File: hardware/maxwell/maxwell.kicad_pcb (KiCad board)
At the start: 2 copper layers, 147 x 59 mm, 127 parts, among them J1 Canbus 1, J10 SPI2_B, J11 BACKUP, J12 UART4, J14 Interconnect (Power), J15 I2C1, J16 ESP_BM, J17 ESP_PROG, J18 Interconnect (Power-Rect), J19 Interconnect (Rect), J2 SPI2_C, J20 Interconnect (uC), J3 Neopixel, J4 BOOT0, J5 SPI2_A, J6 Programmer, J7 Dynamo, J8 BOOT1, J9 Battery, Q1 DMG2302UK, Q2 DMG2302UK, Q3 DMG9926UDM, Q4 NTR1P02T1, Q5 NTR1P02T1, Q6 DMG2302UK, Q7 DMG2302UK, Q8 DMG2302UK, Q9 DMG2302UK, SW1 SW_Push, U1 MCP1501, U10 MIC39102, U11 AP9101C-SOT-25, U12 INA219AID, U13 PCF8593, U14 TPS22917, U15 LM74670-Q1, U16 LM74670-Q1, U17 LM74670-Q1, U18 LM74670-Q1, U19 LT3086IR, U2 SN65HVD233, U20 BQ21040DBVT, U3 TPS2113, U4 PCA9536D, U5 ESP-32S, U6 AD7991, U7 STM32F103RETx, U8 TLP188, U9 MCP79411-I/SN, Y1 32.768k, Y2 8M

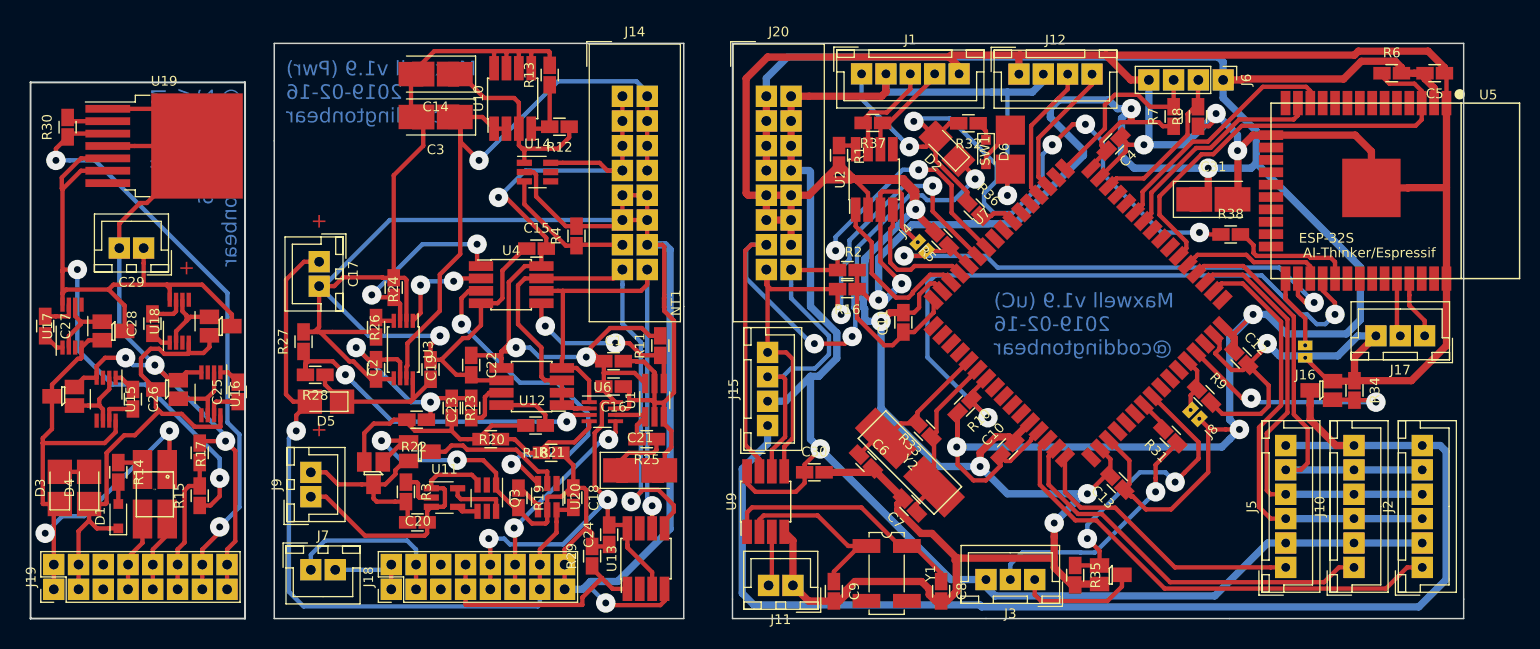
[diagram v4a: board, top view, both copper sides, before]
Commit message: Maxwell v1.9.1
While sciencing earlier today, I narrowed down my surprisingly-high
quiescent current problem to being how I've handled switching
off the Neopixels and SPI-connected devices.  Historicaly,
those were switched using a low-side N-Channel MOSFET. With these
changes, these will be switched via a high-side P-Channel MOSFET
(itself controlled by an N-Channel MOSFET to ensure that the
microcontroller isn't exposed to VCC).

* Swaps Neopixel power-off device from low-side N-Channel MOSFET
  to P-Channel MOSFET controlled by an N-Channel MOSFET.
* Swaps SPI power-off device from low-side N-Channel MOSFET
  to P-Channel MOSFET controlled by an N-Channel MOSFET.
* Fixes a few erroneous resistor values.
* Adds a diode between RTC and WAKE to prevent RTC from being
  able to turn off the power, only turn it on.

* Switches off
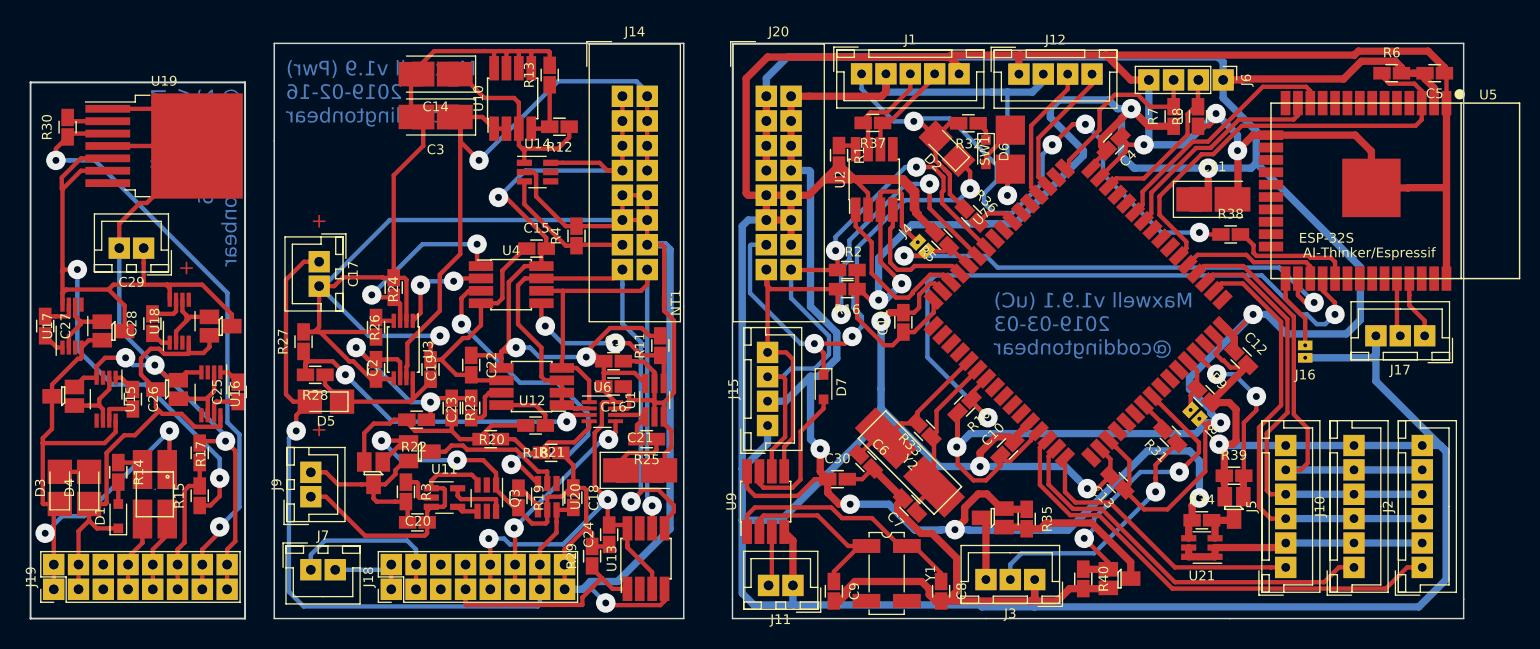
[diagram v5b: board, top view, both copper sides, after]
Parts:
- added D7: 1N4148WS, Diode_SMD:D_SOD-323_HandSoldering, F.Cu at (113.3, 108.3)
- added Q10: NDS332P, coddingtonbear:SOT-23_LargePads, F.Cu at (130.7, 121.7)
- added R39: 10k, coddingtonbear:0805_Milling, F.Cu at (155.4, 117.3)
- added R40: 10k, coddingtonbear:0805_Milling, F.Cu at (140.0, 127.9)
- added U21: STT3P2UH7, Package_TO_SOT_SMD:SOT-23-6_Handsoldering, F.Cu at (152.1, 124.7)
- D6: value D -> 1N4148WS
- R32, R36: value 10k -> 300
- moved R34 20.6 mm to (152.1, 121.9), turned to 0 degrees
- moved Q1 15.0 mm to (155.4, 120.7), turned to 270 degrees
- moved R35 7.61 mm to (134.2, 121.8)
- moved C30 2.47 mm to (114.8, 117.7)
- moved Q2 0.98 mm to (143.7, 127.9)
- moved R36 0.73 mm to (128.5, 90.7)
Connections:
- J10 pad 2: VCC_B -> Net-(J10-Pad2)
- J10 pad 6: /GNDAUX -> GND_B
- J15 pad 1: /GNDAUX -> GND_B
- J2 pad 2: VCC_B -> Net-(J10-Pad2)
- J2 pad 6: /GNDAUX -> GND_B
- J3 pad 1: Net-(J3-Pad1) -> GND_B
- J3 pad 3: VCC_B -> Net-(J3-Pad3)
- J5 pad 2: VCC_B -> Net-(J10-Pad2)
- J5 pad 6: /GNDAUX -> GND_B
- Q1 pad 3: /GNDAUX -> Net-(Q1-Pad3)
- Q2 pad 3: Net-(J3-Pad1) -> Net-(Q10-Pad1)
- R34 pad 1: GND_B -> VCC_B
- R34 pad 2: ENABLE_AUX -> Net-(Q1-Pad3)
- R35 pad 1: ENABLE_LEDS -> VCC_B
- R35 pad 2: GND_B -> Net-(Q10-Pad1)
- U9 pad 7: WAKE_B -> Net-(D7-Pad2)
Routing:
- net /GNDAUX: track 130.7 -> 0.00 mm
- net GND_B: track 453.0 -> 583.2 mm, vias 9 -> 7
- net Net-(J10-Pad2): track 0.00 -> 26.0 mm
- net WAKE_B: track 72.3 -> 50.7 mm
- net Net-(Q10-Pad1): track 0.00 -> 16.7 mm
- net Net-(D7-Pad2): track 0.00 -> 15.2 mm
- net Net-(J3-Pad1): track 12.6 -> 0.00 mm
- net Net-(J3-Pad3): track 0.00 -> 6.52 mm
- net ENABLE_AUX: track 25.1 -> 19.7 mm
- net VCC_B: track 173.9 -> 169.2 mm, vias 2 -> 5
- net Net-(Q1-Pad3): track 0.00 -> 4.34 mm
- net ESP_AVAILABLE: track 78.3 -> 74.6 mm, vias 5 -> 4
- net +3V3_B: track 350.5 -> 349.2 mm
- net Net-(R36-Pad2): track 3.64 -> 4.19 mm
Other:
- board text added: "Maxwell v1.9.1 (uC) 2019-03-03 @coddingtonbear"
- board text removed: "Maxwell v1.9 (uC) 2019-02-16 @coddingtonbear"

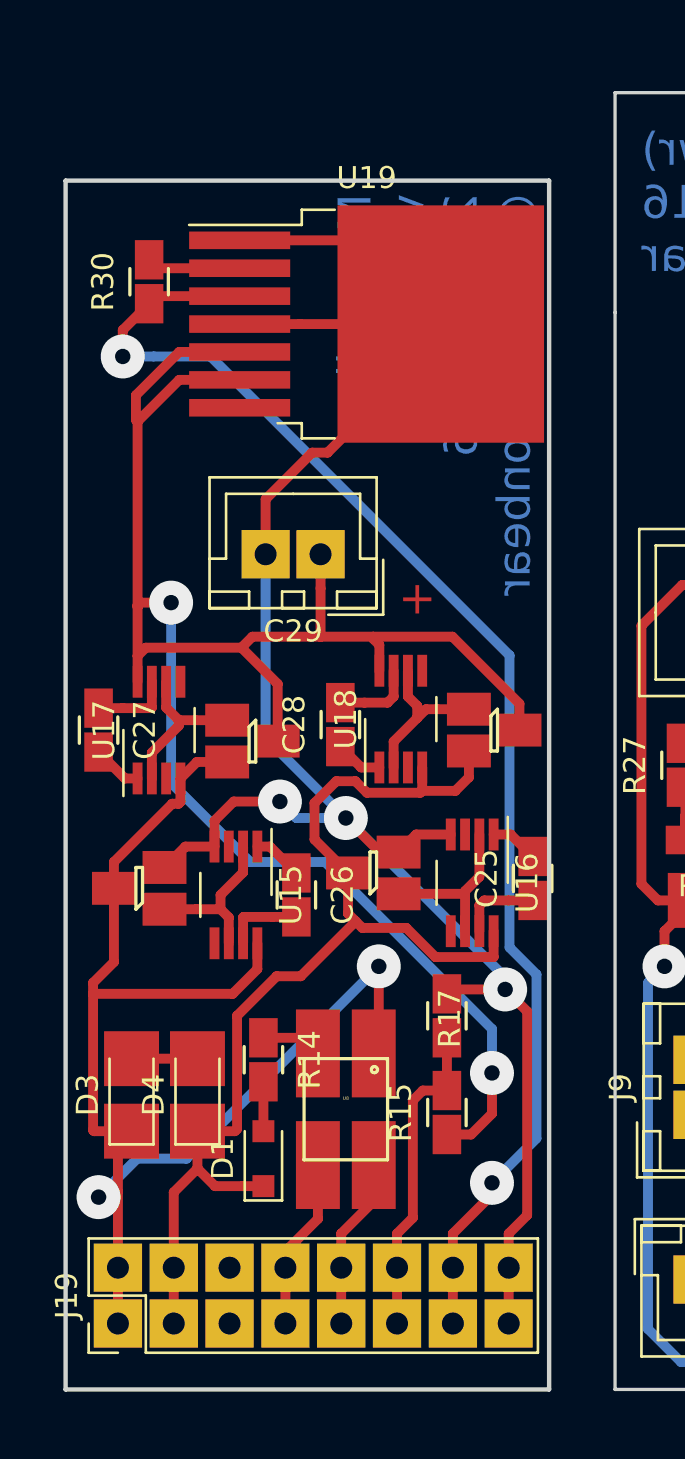
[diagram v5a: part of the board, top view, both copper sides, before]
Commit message: Maxwell v1.9.2
Over the last month, I've melted the voltage cap zeners
off of the rectifier board. This is not great; they serve
an essential purpose in preventing the mosfets and active
rectifiers behind it from being exposed to an overvoltage
situation and burning out (which has happened to at least
one mosfet).

* Uses much bigger DO-201AE package through-hole diodes.
  These should be able to dissapate a lot more heat, and
  if they do heat up the solder enough to begin melting
  at least they won't be able to fall out of position.
* Adds a P-Ch mosfet between the rectifier and capacitor;
  this should allow me to programmatically turn off the
  dynamo power source when I'm travelling very slowly
  or heading uphill.
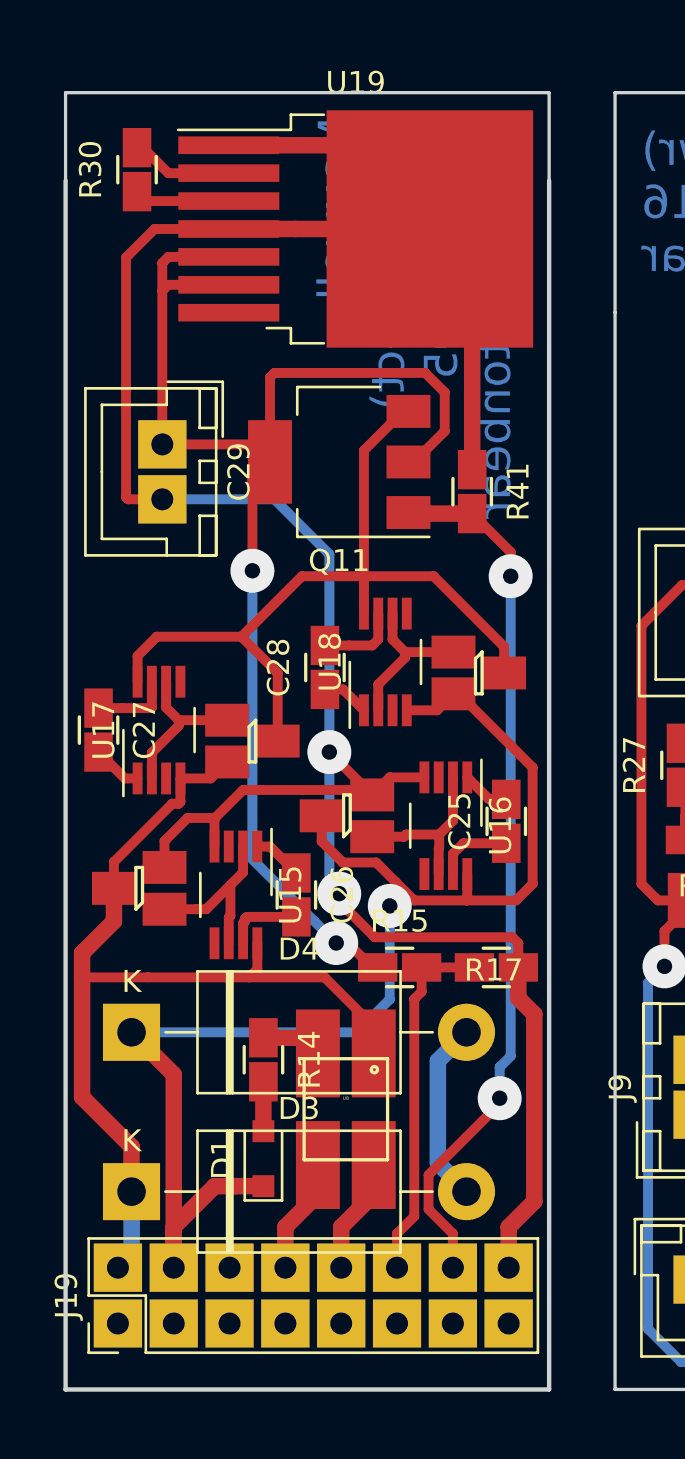
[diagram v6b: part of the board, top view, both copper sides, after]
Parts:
- added Q11: Q_PMOS_GDSD, Package_TO_SOT_SMD:SOT-223, F.Cu at (44.5, 89.8)
- added R41: 10k, coddingtonbear:0805_Milling, F.Cu at (50.5, 91.2)
- D3, D4: footprint coddingtonbear:D_SOD-123_LargePads -> Diode_THT:D_DO-201AE_P15.24mm_Horizontal
- moved C29 8.77 mm to (36.4, 89.0), turned to 270 degrees
- moved R15 6.94 mm to (47.2, 112.8), turned to 0 degrees
- moved R30 5.13 mm to (35.2, 76.5)
- moved D3 4.40 mm to (35.0, 123.0), turned to 0 degrees
- moved U19 4.35 mm to (45.2, 79.2)
- moved D4 4.14 mm to (35.0, 115.8), turned to 0 degrees
- moved R17 3.15 mm to (51.6, 112.8), turned to 180 degrees
- moved U16 2.86 mm to (49.3, 106.3)
- moved C25 2.86 mm to (52.0, 106.2)
- moved Q7 2.86 mm to (44.8, 105.9)
- moved C28 2.69 mm to (43.8, 99.2)
- moved Q9 2.69 mm to (50.8, 99.4)
- moved U18 2.69 mm to (46.5, 98.9)
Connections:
- J19 pad 13: VDYN_C -> DISABLE_DYNAMO
- J19 pad 14: VDYN_C -> DISABLE_DYNAMO
- J19 pad 6: Net-(J19-Pad6) -> Net-(J19-Pad5)
- Q8 pad 3: Net-(C29-Pad1) -> Net-(Q11-Pad3)
- Q9 pad 3: Net-(C29-Pad1) -> Net-(Q11-Pad3)
- R30 pad 1: VDYN_C -> Net-(R30-Pad1)
- U17 pad 8: Net-(C29-Pad1) -> Net-(Q11-Pad3)
- U18 pad 8: Net-(C29-Pad1) -> Net-(Q11-Pad3)
- U19 pad 3: VDYN_C -> Net-(R30-Pad1)
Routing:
- net VDYN_C: track 62.9 -> 0.00 mm, vias 2 -> 0
- net DISABLE_DYNAMO: track 0.00 -> 40.0 mm, vias 0 -> 2
- net Net-(Q11-Pad3): track 0.00 -> 37.5 mm
- net Net-(C29-Pad1): track 90.0 -> 62.2 mm
- net GND_C: track 93.3 -> 117.0 mm, vias 3 -> 2
- net V_AC+: track 62.3 -> 45.0 mm, vias 2 -> 0
- net V_AC-: track 51.2 -> 62.2 mm, vias 0 -> 1
- net Net-(D3-Pad2): track 3.00 -> 8.33 mm
- net Net-(R30-Pad1): track 0.00 -> 4.35 mm
- net +3V3_C: track 7.82 -> 5.28 mm
- net DYNAMO_POLE_SIG_C: track 7.82 -> 5.28 mm
- net DYNAMO_VOLTAGE_C: track 14.6 -> 16.5 mm
- net Net-(Q6-Pad1): track 7.53 -> 8.12 mm
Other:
- outline, holes or cut-outs redrawn
- board text added: "Maxwell v1.9.2 (Rect) 2019-04-05 @coddingtonbear"
- board text removed: "Maxwell v1.9 (Rect) 2019-02-16 @coddingtonbear"
